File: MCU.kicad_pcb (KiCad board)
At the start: 2 copper layers, 15 parts, among them M1 Conn_01x04, M2 Conn_01x04, M3 Conn_01x04, U2 ESP32-S3-DevKitC

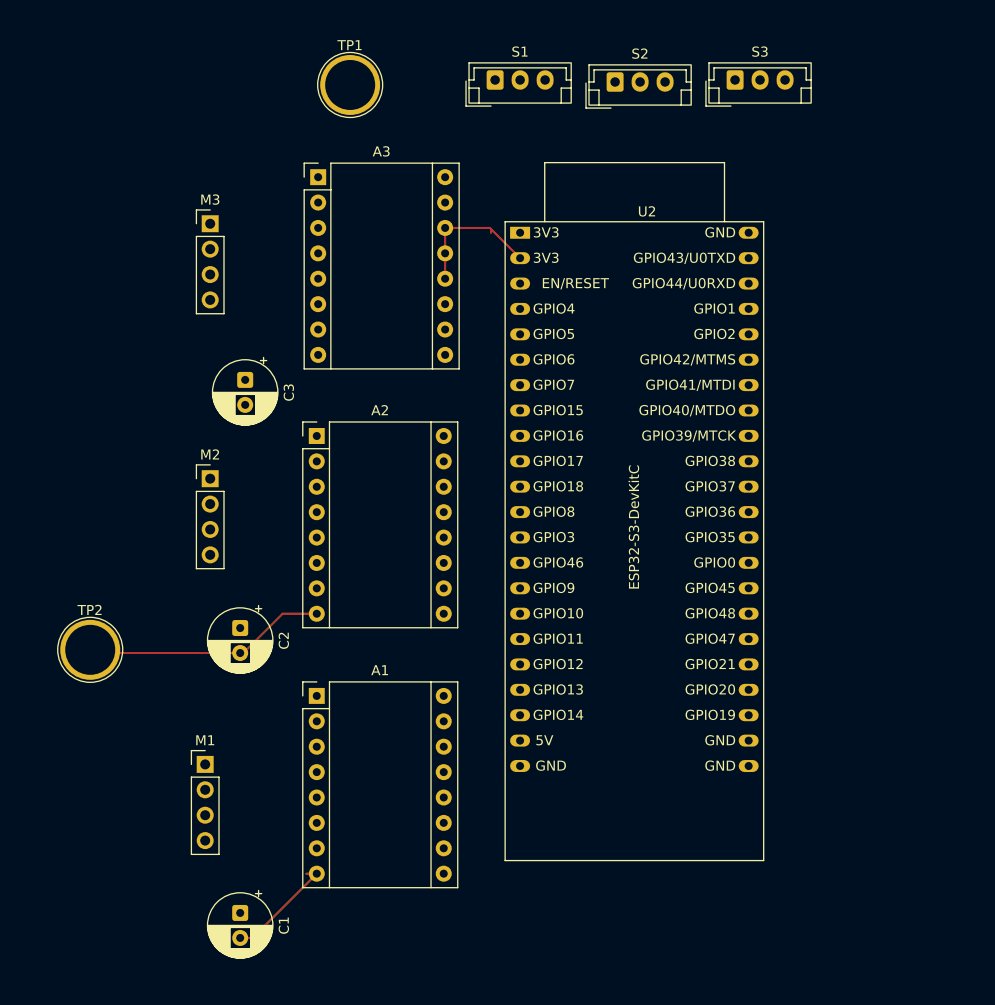
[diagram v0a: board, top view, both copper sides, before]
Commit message: Changed routings and added encoder ports (pwm output pins).
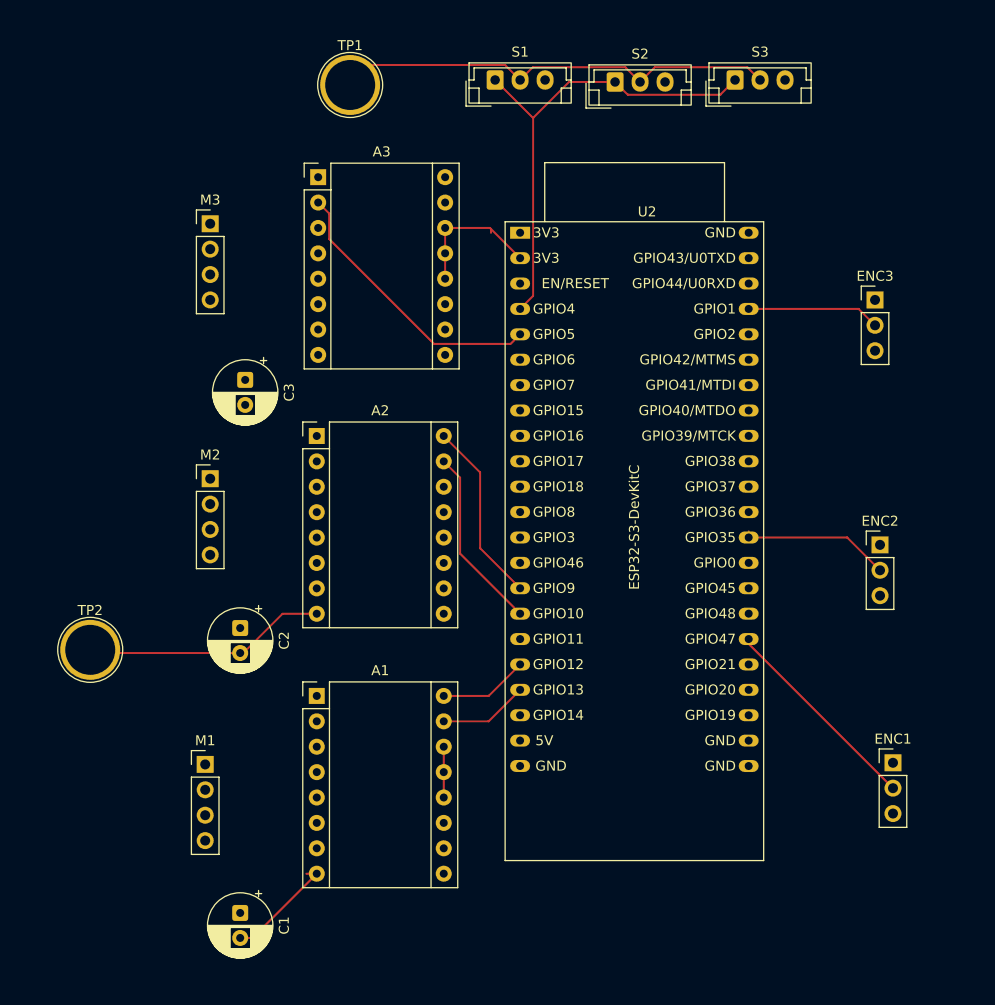
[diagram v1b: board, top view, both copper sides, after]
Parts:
- added ENC1: Conn_01x03, Connector_PinHeader_2.54mm:PinHeader_1x03_P2.54mm_Vertical, F.Cu at (110.8, 148.8)
- added ENC2: Conn_01x03, Connector_PinHeader_2.54mm:PinHeader_1x03_P2.54mm_Vertical, F.Cu at (109.5, 127.0)
- added ENC3: Conn_01x03, Connector_PinHeader_2.54mm:PinHeader_1x03_P2.54mm_Vertical, F.Cu at (109.0, 102.5)
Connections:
- C1 pad 2: +12V -> unconnected-(C1-Pad2)
- U2 pad 28: unconnected-(U2-GPIO47-Pad28) -> ENC_OUT1
- U2 pad 32: unconnected-(U2-GPIO35-Pad32) -> ENC_OUT2
- U2 pad 41: unconnected-(U2-GPIO1/ADC1_CH0-Pad41) -> ENC_OUT3
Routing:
- net UART_DATA: track 0.00 -> 47.8 mm
- net +7.5V: track 0.00 -> 44.7 mm
- net FAULT3: track 0.00 -> 27.9 mm
- net ENC_OUT1: track 0.00 -> 20.9 mm
- net M2DIR: track 0.00 -> 18.4 mm
- net M2STEP: track 0.00 -> 18.4 mm
- net ENC_OUT2: track 0.00 -> 15.1 mm
- net ENC_OUT3: track 0.00 -> 13.3 mm
- net M1STEP: track 0.00 -> 8.94 mm
- net M1DIR: track 0.00 -> 8.94 mm
- net +3.3V: track 14.2 -> 19.3 mm

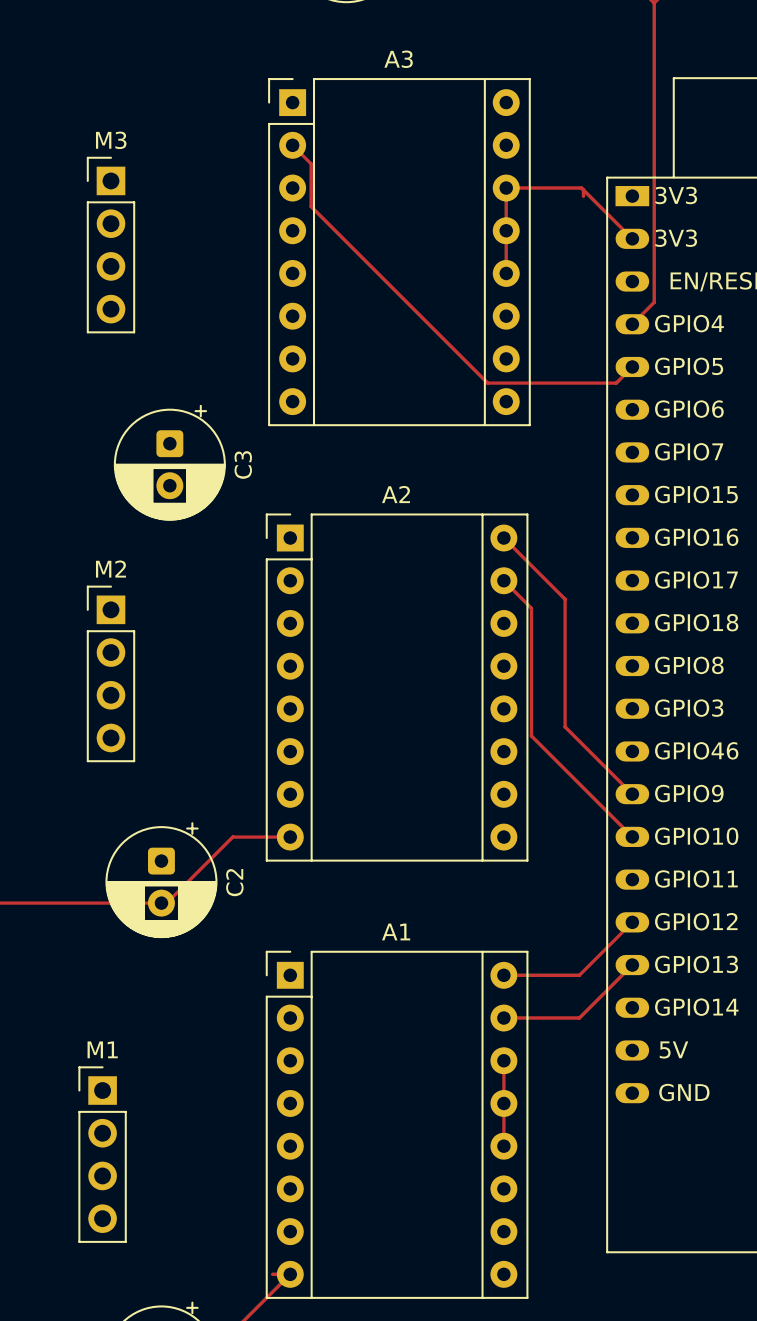
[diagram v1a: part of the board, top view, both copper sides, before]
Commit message: finished trace wiring on PCB
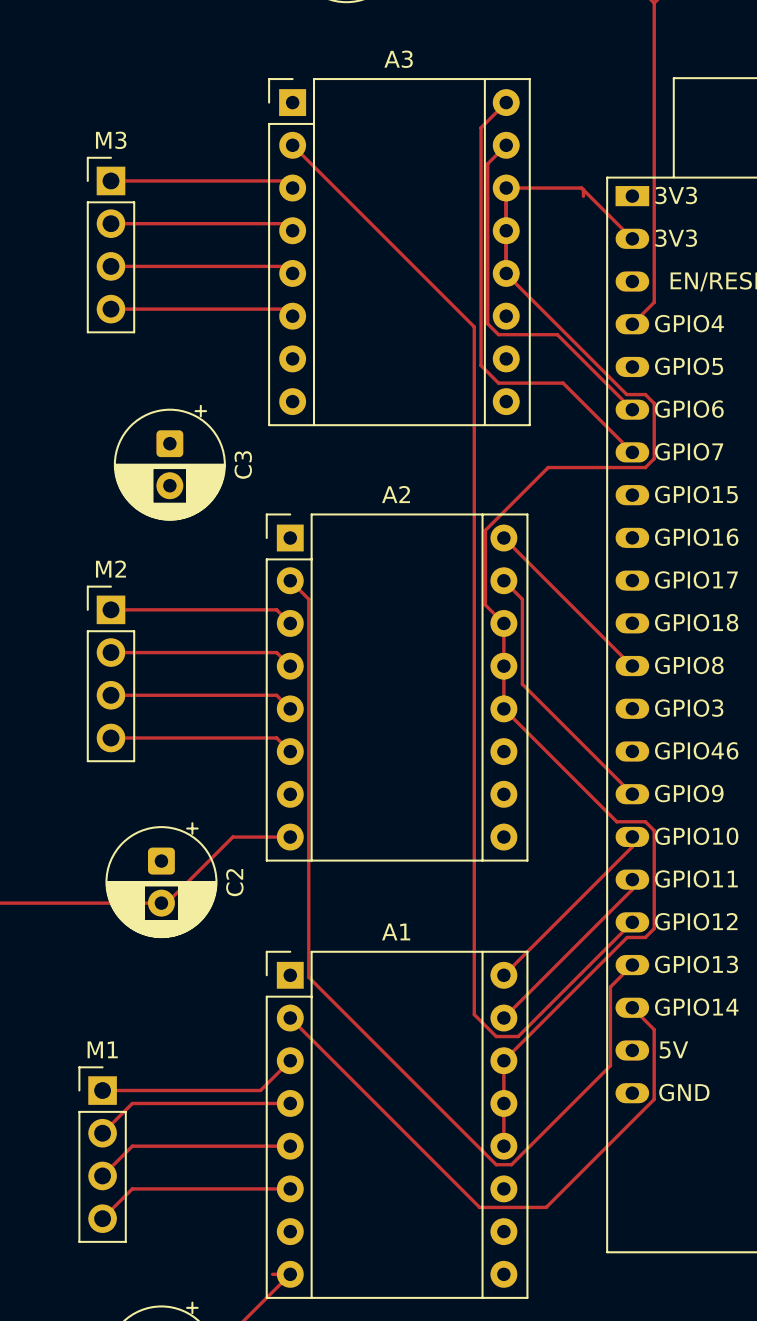
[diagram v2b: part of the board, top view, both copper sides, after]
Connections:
- M1 pad 1: Net-(A1-A1) -> Net-(A1-A2)
- M1 pad 2: Net-(A1-A2) -> Net-(A1-A1)
- M2 pad 1: Net-(A2-A1) -> Net-(A2-A2)
- M2 pad 2: Net-(A2-A2) -> Net-(A2-A1)
- M3 pad 1: Net-(A3-A1) -> Net-(A3-A2)
- M3 pad 2: Net-(A3-A2) -> Net-(A3-A1)
- U2 pad 12: FAULT2 -> M2DIR
- U2 pad 15: M2DIR -> M2STEP
- U2 pad 16: M2STEP -> M1DIR
- U2 pad 17: FAULT1 -> M1STEP
- U2 pad 18: M1DIR -> FAULT3
- U2 pad 19: M1STEP -> FAULT2
- U2 pad 20: unconnected-(U2-GPIO14/ADC2_CH3-Pad20) -> FAULT1
- U2 pad 5: FAULT3 -> unconnected-(U2-GPIO5/ADC1_CH4-Pad5)
- U2 pad 6: M3DIR -> M3STEP
- U2 pad 7: M3STEP -> M3DIR
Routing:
- net +3.3V: track 19.3 -> 92.5 mm
- net FAULT2: track 0.00 -> 55.5 mm
- net FAULT3: track 27.9 -> 68.9 mm
- net FAULT1: track 0.00 -> 35.0 mm
- net M3DIR: track 0.00 -> 27.4 mm
- net M3STEP: track 0.00 -> 21.8 mm
- net Net-(A1-A1): track 0.00 -> 12.4 mm
- net Net-(A1-A2): track 0.00 -> 11.9 mm
- net Net-(A1-B2): track 0.00 -> 11.9 mm
- net Net-(A1-B1): track 0.00 -> 11.9 mm
- net Net-(A2-B2): track 0.00 -> 11.0 mm
- net Net-(A2-B1): track 0.00 -> 11.0 mm
- net Net-(A2-A2): track 0.00 -> 11.0 mm
- net Net-(A2-A1): track 0.00 -> 11.0 mm
- net Net-(A3-B2): track 0.00 -> 11.0 mm
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
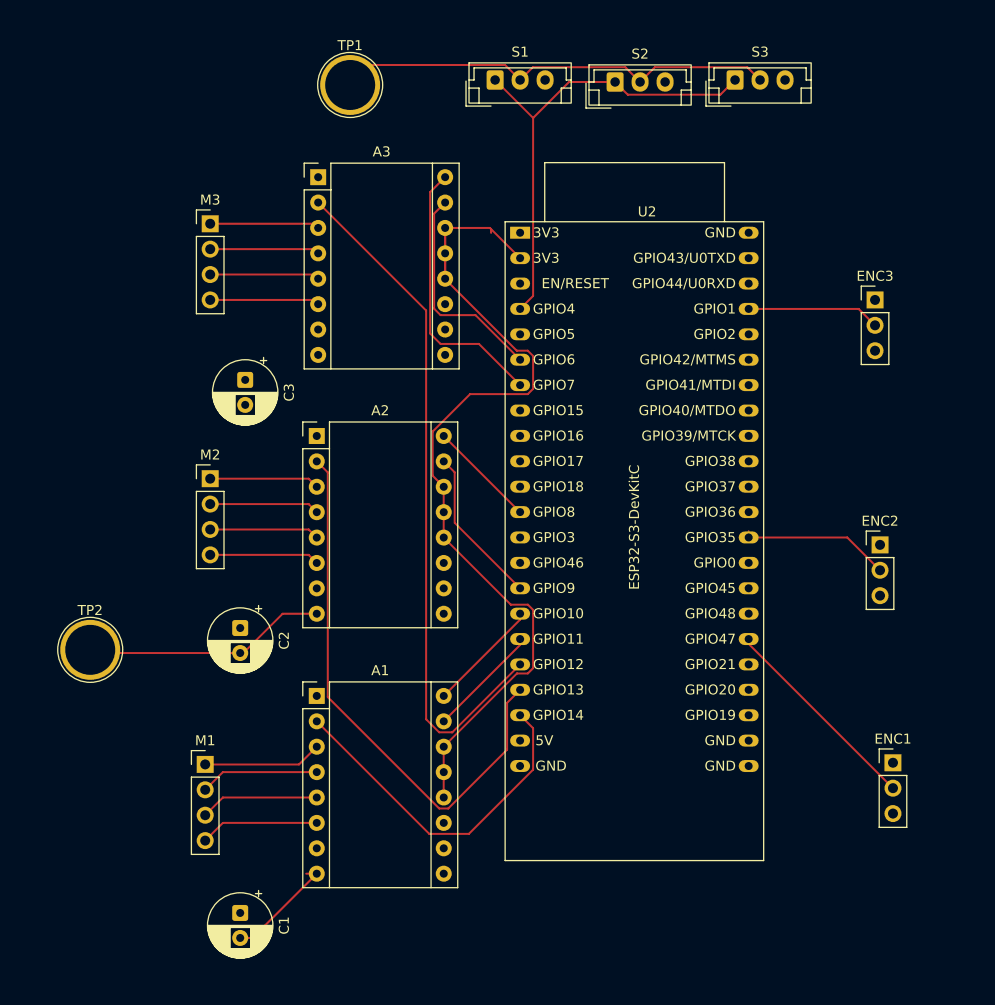
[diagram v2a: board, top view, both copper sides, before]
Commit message: fixed trace widths
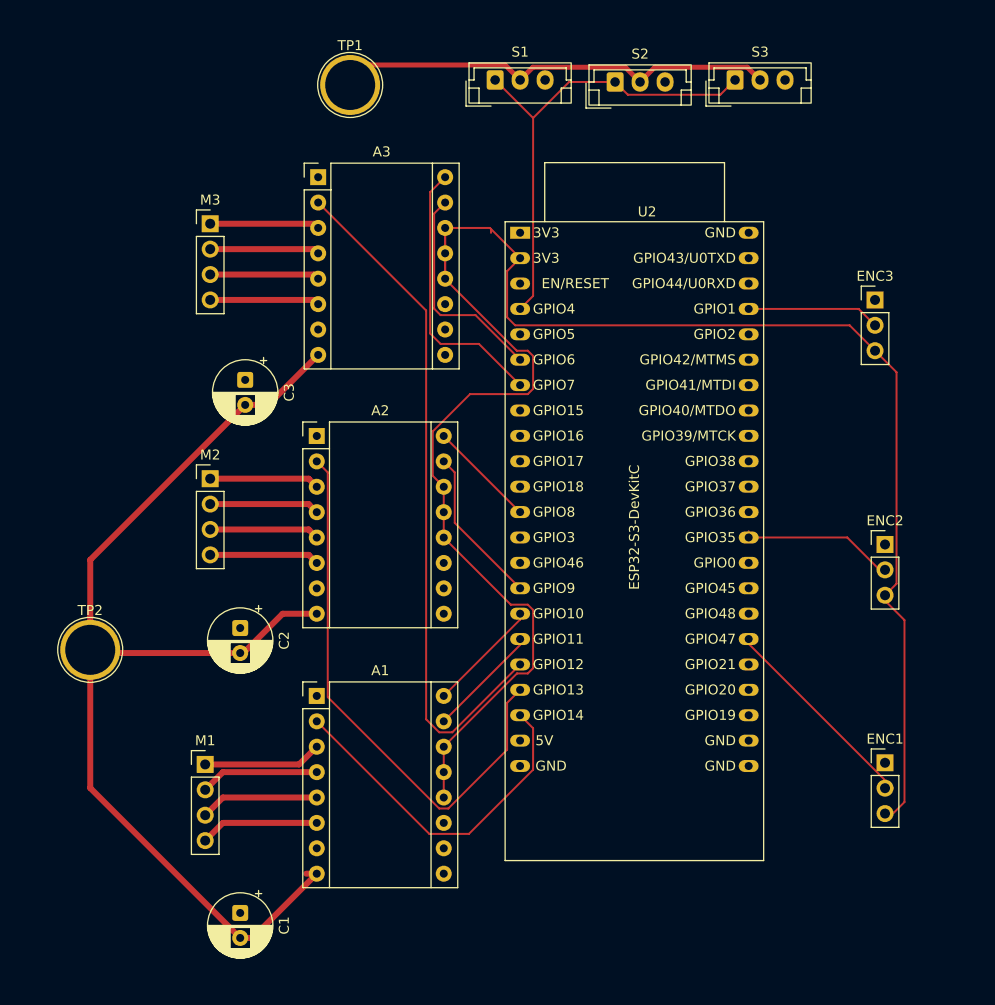
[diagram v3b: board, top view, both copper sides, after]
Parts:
- moved ENC1 0.80 mm to (110.0, 148.8)
- moved ENC2 0.50 mm to (110.0, 127.0)
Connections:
- C1 pad 2: unconnected-(C1-Pad2) -> +12V
- ENC1 pad 3: +3V3 -> +3.3V
- ENC2 pad 3: +3V3 -> +3.3V
- ENC3 pad 3: +3V3 -> +3.3V
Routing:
- net +3.3V: track 92.5 -> 186.3 mm
- net +12V: track 35.8 -> 111.1 mm

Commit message: completed board, ready for review, if passes review, ready to print
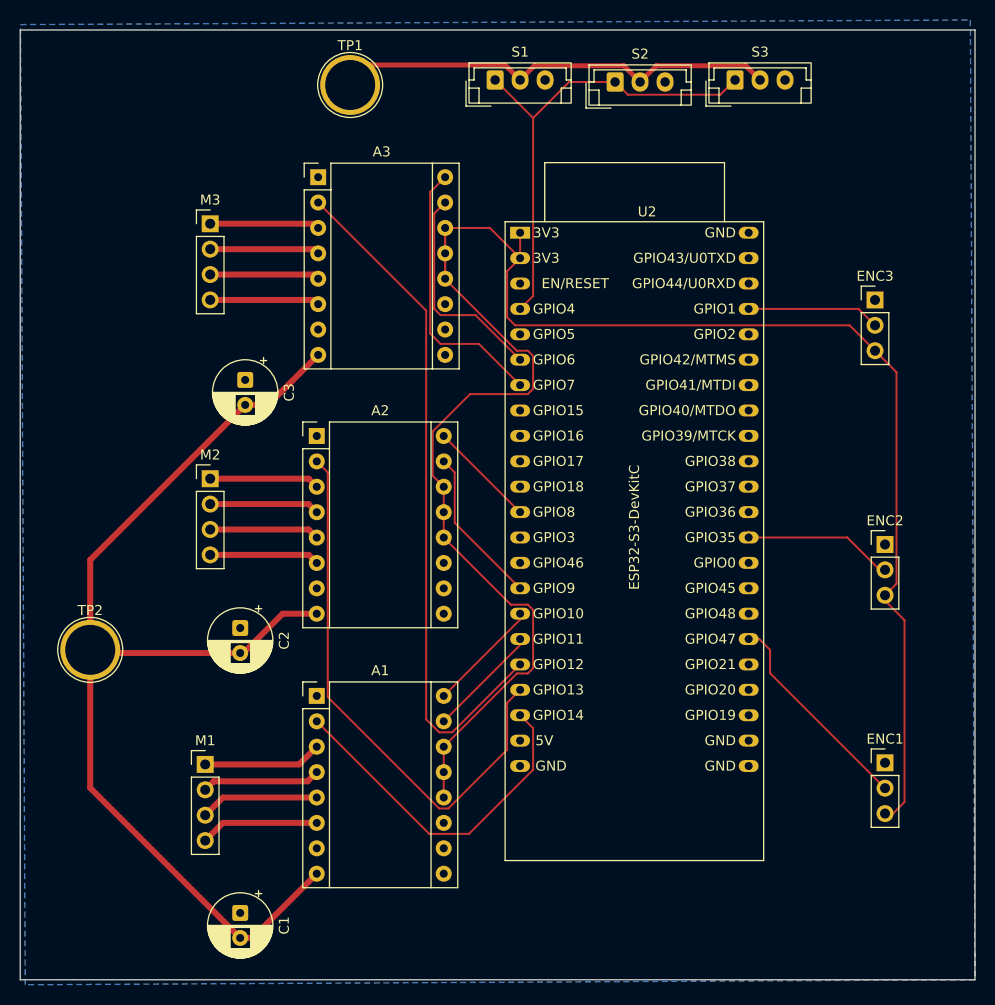
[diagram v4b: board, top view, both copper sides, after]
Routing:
- net +3.3V: track 186.3 -> 188.4 mm
- net +12V: track 111.1 -> 110.1 mm
- net ENC_OUT1: track 20.9 -> 21.7 mm
- added copper zone on B.Cu, net GND
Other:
- board outline added: 95.5 x 95 mm
- board text added: "6DoF Telebuddy"
- board text added: "Hunching Hobos"

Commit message: forgot to add these
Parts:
- added G***: LOGO, assets:hobonew, F.Cu at (31.5, 93.0)

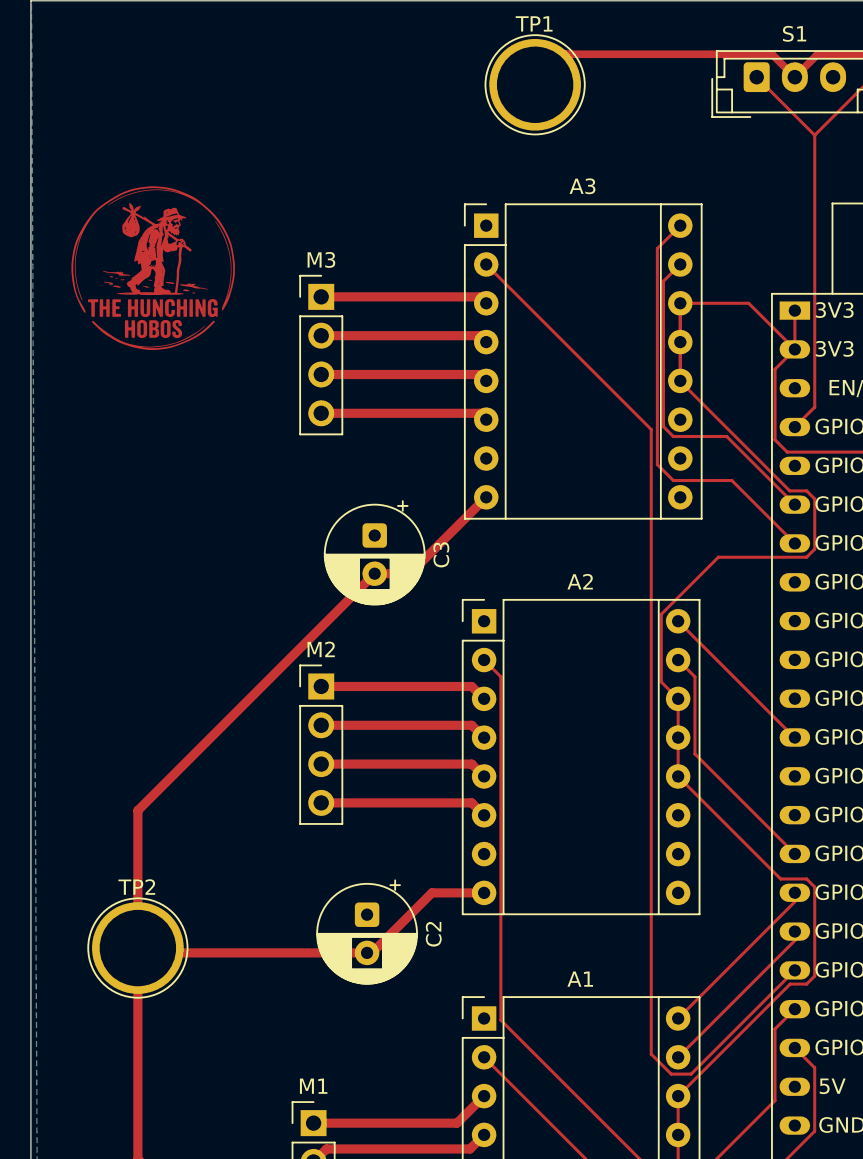
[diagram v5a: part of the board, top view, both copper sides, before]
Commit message: changed logo footprint and capacitor spacing and labels
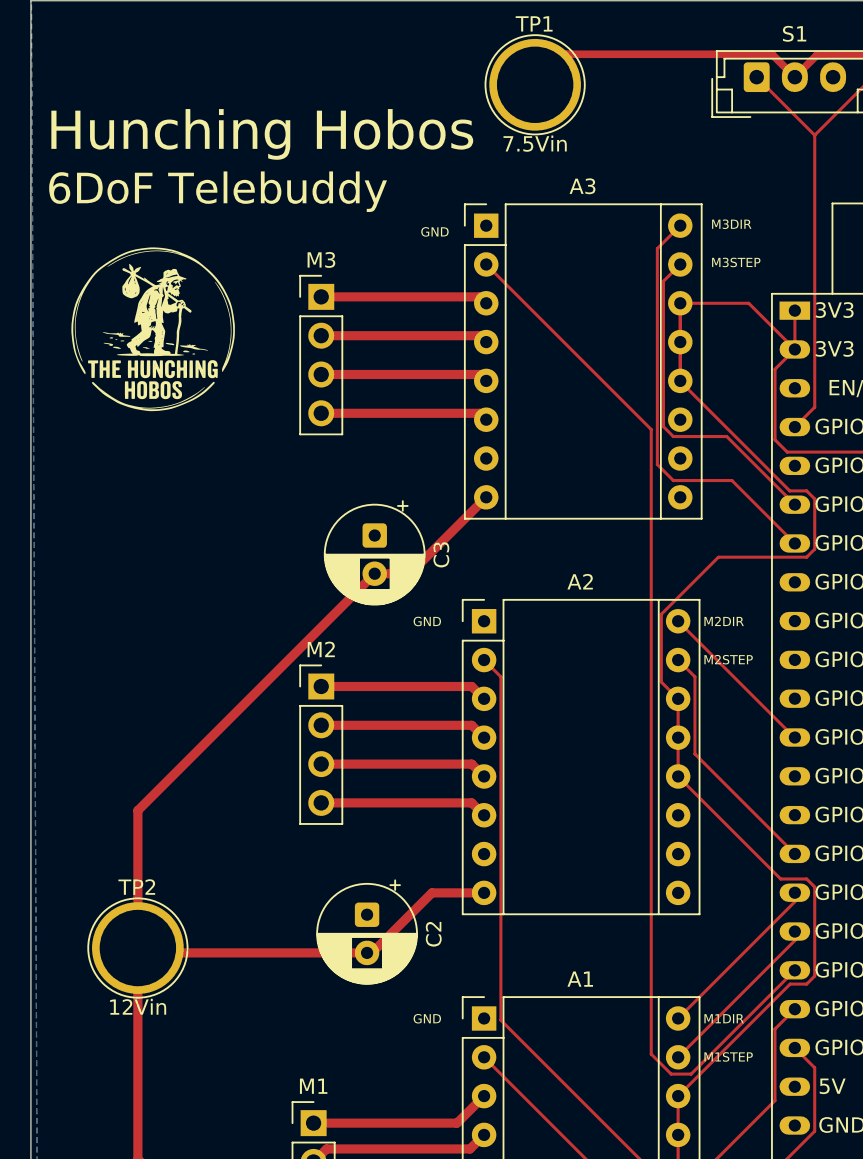
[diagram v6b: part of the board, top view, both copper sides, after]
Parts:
- moved G*** 4.00 mm to (31.5, 97.0)
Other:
- board text added: "GND"
- board text added: "M1DIR"
- board text added: "M1STEP"
- board text added: "M2DIR"
- board text added: "M2STEP"
- board text added: "M3DIR"
- board text added: "M3STEP"
